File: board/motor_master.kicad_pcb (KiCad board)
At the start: 2 copper layers, 42 x 52 mm, 38 parts, among them IC1 LM1117MPX-3.3_NOPB, IC2 SN65HVD232DR, J1 PWR, J2 USB4105-GF-A, J3 FTDI, J4 CAN, J5 TERM, J6 PWM1, J7 PWM2, U1 ESP32-S3-WROOM-1-N8

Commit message: Board revisions from design review
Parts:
- added C13: 0.1uF, Capacitor_SMD:C_0603_1608Metric, F.Cu at (167.5, 122.0)
- added C14: 4.7n, Capacitor_SMD:C_0603_1608Metric, F.Cu at (167.5, 106.5)
- added C15: 100p, Capacitor_SMD:C_0603_1608Metric, F.Cu at (170.0, 106.0)
- added C9: 100p, Capacitor_SMD:C_0603_1608Metric, F.Cu at (165.0, 106.0)
- added D5: 150060RS75000, SamacSys_Parts:LEDC1608X80N, F.Cu at (171.5, 113.5)
- added D6: SZNUP2105LT1G, SamacSys_Parts:SOT96P237X111-3N, F.Cu at (167.5, 103.0)
- added J1: EXT, SamacSys_Parts:TSW-102-XX-YY-S, F.Cu at (128.8, 84.2)
- added R10: 47, Resistor_SMD:R_0603_1608Metric, F.Cu at (171.5, 118.2)
- added R2: 10k, Resistor_SMD:R_0603_1608Metric, F.Cu at (132.0, 82.0)
- added REF**: MountingHole_2.2mm_M2_Pad, MountingHole:MountingHole_2.2mm_M2_Pad, F.Cu at (170.0, 77.0)
- added REF**: MountingHole_2.2mm_M2_Pad, MountingHole:MountingHole_2.2mm_M2_Pad, F.Cu at (130.0, 125.5)
- added REF**: MountingHole_2.2mm_M2_Pad, MountingHole:MountingHole_2.2mm_M2_Pad, F.Cu at (130.0, 77.0)
- added REF**: MountingHole_2.2mm_M2_Pad, MountingHole:MountingHole_2.2mm_M2_Pad, F.Cu at (170.0, 125.5)
- D2: renamed from D3; value D5V0S1U2LP-7B -> PTVS18VU1UPAZ; footprint SamacSys_Parts:D5V0S1U2LP7B -> SamacSys_Parts:PMEG6020EPA115
- D4: value D5V0S1U2LP-7B -> PTVS18VU1UPAZ; footprint SamacSys_Parts:D5V0S1U2LP7B -> SamacSys_Parts:PMEG6020EPA115
- J4, J6, J7: footprint SamacSys_Parts:TSW-103-XX-YY-S -> SamacSys_Parts:1719710103
- J5: renamed from J1; value PWR -> 5-12V; footprint SamacSys_Parts:SHDR2W70P0X500_1X2_1000X750X1160P -> SamacSys_Parts:1190297
- J8: renamed from J5; footprint SamacSys_Parts:RHDR3W79P0X254_1X3_813X241X851P -> SamacSys_Parts:1719710103
- R1: renamed from R3; value 5.1k -> 47
- R8: value 10k -> 60; footprint Resistor_SMD:R_0603_1608Metric -> Resistor_SMD:R_1206_3216Metric
- R9: renamed from R7; value 120 -> 60; footprint Resistor_SMD:R_0603_1608Metric -> Resistor_SMD:R_1206_3216Metric
- moved IC2 41.1 mm to (167.5, 117.0), turned to 90 degrees
- moved R9 38.6 mm to (166.0, 110.5), turned to -90 degrees
- moved R11 38.5 mm to (167.8, 81.0), turned to 180 degrees
- moved R1 33.9 mm to (131.0, 120.5), turned to 90 degrees
- moved J8 32.7 mm to (164.9, 86.5), turned to 180 degrees
- moved J4 30.3 mm to (165.0, 95.5), turned to 180 degrees
- moved R8 29.6 mm to (169.0, 110.5), turned to -90 degrees
- moved D1 28.6 mm to (134.5, 125.5), turned to -90 degrees
- moved S4 27.0 mm to (162.0, 79.0)
- moved C7 26.2 mm to (137.4, 86.3)
- moved C11 23.5 mm to (158.5, 83.5), turned to 180 degrees
- moved J2 20.4 mm to (161.5, 116.0), turned to 90 degrees
- moved S1 20.0 mm to (136.0, 79.2), turned to -90 degrees
- moved R7 19.7 mm to (158.5, 85.5), turned to 0 degrees
- moved R6 16.4 mm to (160.5, 101.5), turned to -90 degrees
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- renumbered C2 to C1, C11 to C10, C8 to C11, C9 to C12, C1 to C2, C7 to C3, C6 to C4, C4 to C5, C5 to C6, C10 to C7, C3 to C8, D2 to D3, J3 to J2, J2 to J3, R6 to R11, R2 to R3, R1 to R4, R9 to R6, R4 to R7, S4 to S1, S3 to S2, S1 to S3, S2 to S4
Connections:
- C11 pad 2: GPIO15 -> GPIO48
- C7 pad 2: GPIO4 -> GPIO2
- D2 pad 1: VCC_IN -> Net-(D2-A_1)
- D2 pad 2: Net-(D2-IO1) -> Net-(D2-A_1)
- D3 pad 1: Net-(D2-IO1) -> Net-(D2-A_1)
- D4 pad 1: VCC_IN -> Net-(D4-A_1)
- D4 pad 2: Net-(D4-A) -> Net-(D4-A_1)
- IC2 pad 1: GPIO12 -> GPIO9
- IC2 pad 4: GPIO13 -> GPIO10
- IC2 pad 6: Net-(IC2-CANL) -> Net-(D6-CANL)
- J2 pad 2: Net-(D4-A) -> Net-(D4-A_1)
- J3 pad A4_B9: Net-(D2-IO1) -> Net-(D2-A_1)
- J3 pad B4_A9: Net-(D2-IO1) -> Net-(D2-A_1)
- J4 pad 2: unconnected-(J4-NC-Pad2) -> GND
- J4 pad 3: Net-(IC2-CANL) -> Net-(D6-CANL)
- J5 pad 2: GND -> VCC_IN
- J6 pad 1: GPIO5 -> GPIO21
- J7 pad 1: GPIO6 -> GPIO47
- J8 pad 2: unconnected-(J5-NC-Pad2) -> GND
- R7 pad 1: GPIO15 -> GPIO48
- R8 pad 1: GPIO4 -> Net-(C14-Pad2)
- R8 pad 2: VCC_3V3 -> Net-(D6-CANL)
- R9 pad 1: Net-(IC2-CANL) -> Net-(C14-Pad2)
- S1 pad 2: GPIO4 -> GPIO2
- S4 pad 2: GPIO15 -> GPIO48
- S4 pad 4: GPIO15 -> GPIO48
- U1 pad 17: unconnected-(U1-IO9-Pad17) -> GPIO9
- U1 pad 18: unconnected-(U1-IO10-Pad18) -> GPIO10
- U1 pad 19: unconnected-(U1-IO11-Pad19) -> GPIO11
- U1 pad 20: GPIO12 -> unconnected-(U1-IO12-Pad20)
- U1 pad 21: GPIO13 -> unconnected-(U1-IO13-Pad21)
- U1 pad 23: unconnected-(U1-IO21-Pad23) -> GPIO21
- U1 pad 24: unconnected-(U1-IO47-Pad24) -> GPIO47
- U1 pad 25: unconnected-(U1-IO48-Pad25) -> GPIO48
- U1 pad 38: unconnected-(U1-IO2-Pad38) -> GPIO2
- U1 pad 39: unconnected-(U1-IO1-Pad39) -> GPIO1
- U1 pad 4: GPIO4 -> unconnected-(U1-IO4-Pad4)
- U1 pad 5: GPIO5 -> unconnected-(U1-IO5-Pad5)
- U1 pad 6: GPIO6 -> unconnected-(U1-IO6-Pad6)
- U1 pad 8: GPIO15 -> unconnected-(U1-IO15-Pad8)
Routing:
- net GPIO4: track 42.3 -> 0.00 mm, vias 2 -> 0
- net GPIO5: track 40.3 -> 0.00 mm, vias 1 -> 0
- net GPIO6: track 31.6 -> 0.00 mm, vias 1 -> 0
- net GPIO10: track 0.00 -> 31.1 mm
- net GPIO11: track 0.00 -> 29.6 mm, vias 0 -> 2
- net GPIO9: track 0.00 -> 26.5 mm
- net GPIO15: track 23.9 -> 0.00 mm, vias 1 -> 0
- net GPIO13: track 21.4 -> 0.00 mm, vias 2 -> 0
- net Net-(D6-CANL): track 0.00 -> 21.3 mm
- net VCC_IN: track 28.9 -> 48.8 mm, vias 0 -> 2
- net GPIO21: track 0.00 -> 18.9 mm, vias 0 -> 2
- net GPIO48: track 0.00 -> 18.9 mm
- net GPIO12: track 17.3 -> 0.00 mm, vias 2 -> 0
- net Net-(D2-IO1): track 17.1 -> 0.00 mm, vias 2 -> 0
- net Net-(D2-A_1): track 0.00 -> 15.1 mm, vias 0 -> 2
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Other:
- board size 42 x 52 mm -> 47 x 55.5 mm
- rule pad_to_mask_clearance: 0.038 -> 0.0508
- board text added: "+"
- board text added: "-"
- board text added: "47x55.5mm"
- board text added: "5-12v"
- board text added: "G"
- board text added: "Robotics Academy 2024 v1"
- board text added: "S"

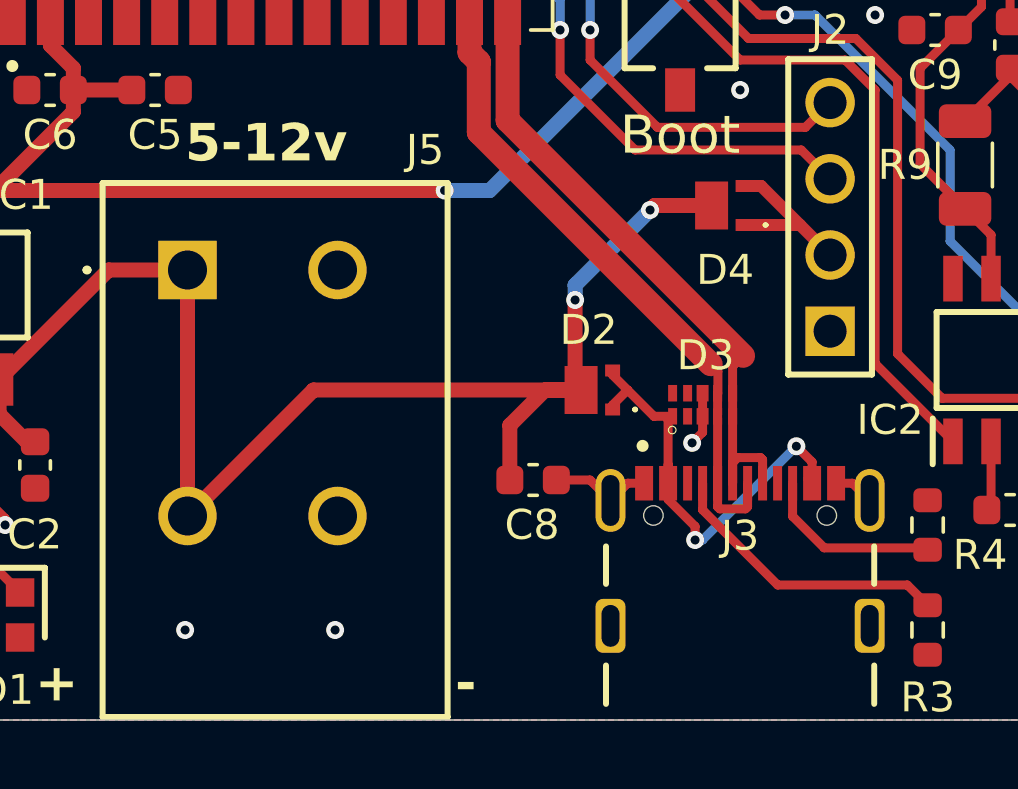
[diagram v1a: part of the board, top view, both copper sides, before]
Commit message: Changed power diodes
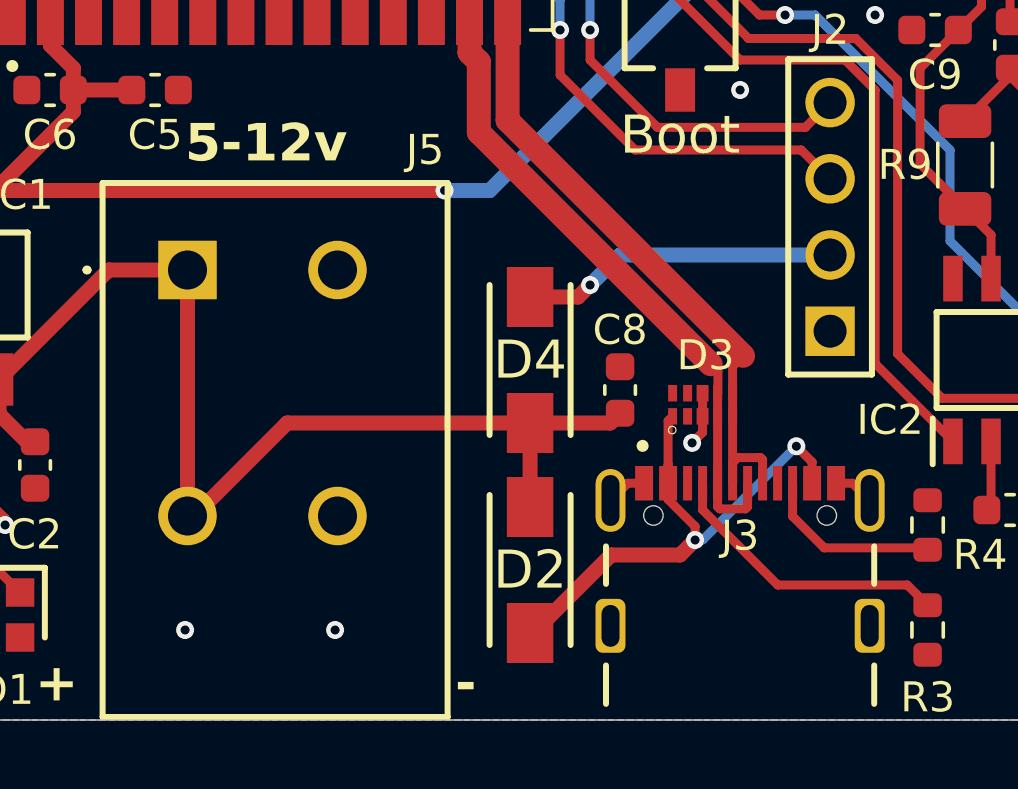
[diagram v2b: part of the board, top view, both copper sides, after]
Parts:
- D2, D4: value PTVS18VU1UPAZ -> SK14; footprint SamacSys_Parts:PMEG6020EPA115 -> SamacSys_Parts:DIONM5027X250N
- moved D4 8.14 mm to (151.5, 117.0)
- moved D2 6.31 mm to (151.5, 124.0), turned to -90 degrees
- moved C8 4.17 mm to (154.5, 118.0), turned to -90 degrees
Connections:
- D2 pad 1: Net-(D2-A_1) -> VCC_IN
- D2 pad 2: Net-(D2-A_1) -> Net-(D2-A)
- D3 pad 1: Net-(D2-A_1) -> Net-(D2-A)
- D4 pad 1: Net-(D4-A_1) -> VCC_IN
- D4 pad 2: Net-(D4-A_1) -> Net-(D4-A)
- J2 pad 2: Net-(D4-A_1) -> Net-(D4-A)
- J3 pad A4_B9: Net-(D2-A_1) -> Net-(D2-A)
- J3 pad B4_A9: Net-(D2-A_1) -> Net-(D2-A)
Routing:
- net Net-(D2-A): track 0.00 -> 18.3 mm, vias 0 -> 2
- net Net-(D2-A_1): track 15.1 -> 0.00 mm, vias 2 -> 0
- net Net-(D4-A): track 0.00 -> 10.6 mm, vias 0 -> 1
- net VCC_IN: track 48.8 -> 38.6 mm, vias 2 -> 0
- net Net-(D4-A_1): track 7.17 -> 0.00 mm
- net GND: track 23.2 -> 21.1 mm

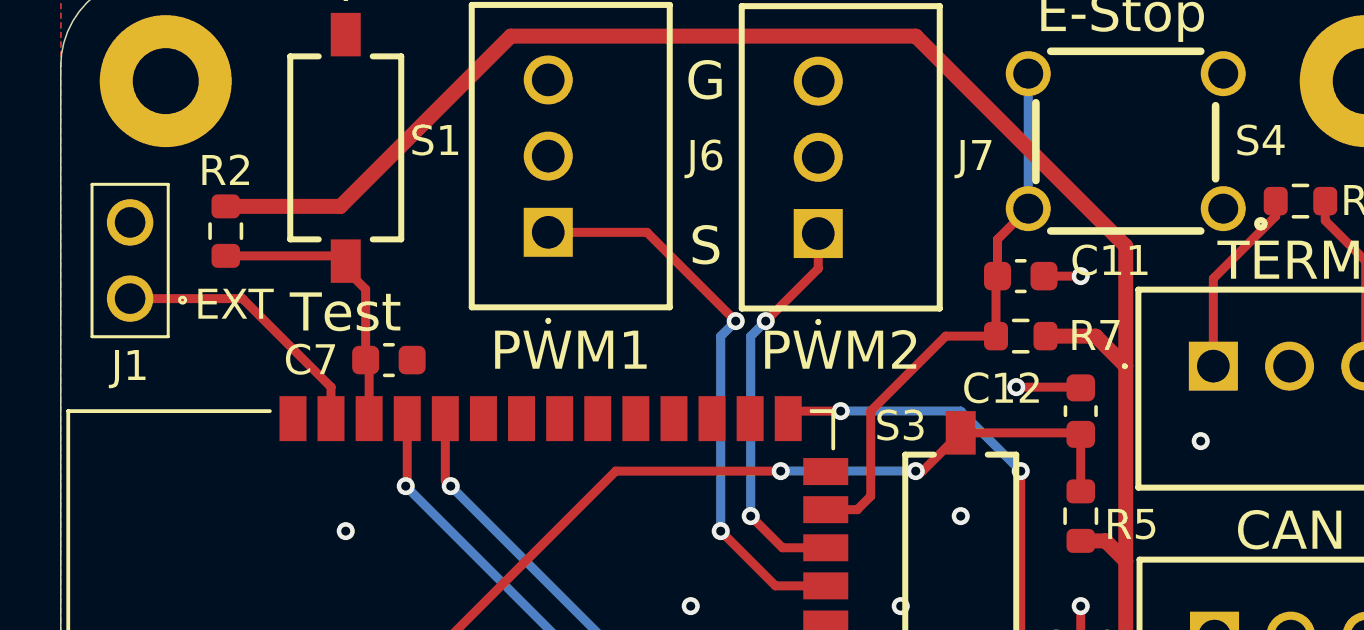
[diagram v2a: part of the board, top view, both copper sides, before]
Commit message: Updated BOM with manufactuer numbers
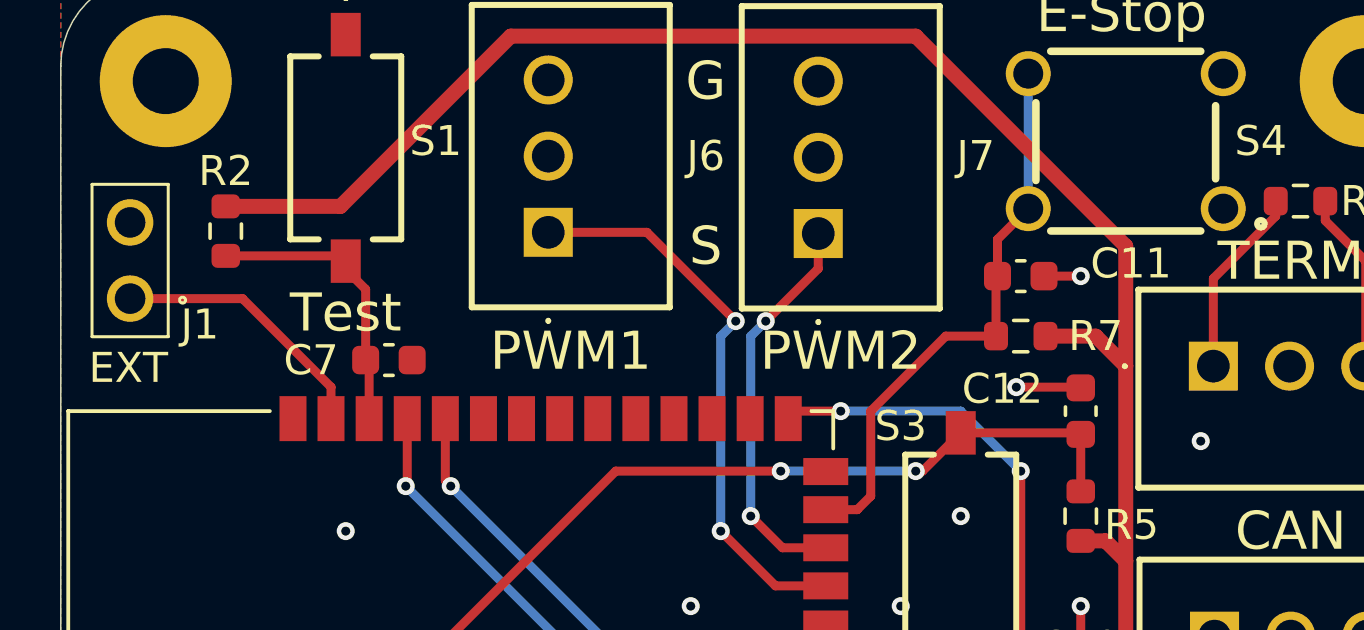
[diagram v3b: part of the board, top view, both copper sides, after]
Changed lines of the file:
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@@
 			(outputformat 1)
 			(mirror no)
-			(drillshape 1)
+			(drillshape 0)
 			(scaleselection 1)
-			(outputdirectory "")
+			(outputdirectory "gerber")
 		)
 	)
@@
 		(tags "Connector")
 		(property "Reference" "J1"
-			(at -2.25 0 180)
+			(at -0.865071 2.324069 180)
 			(layer "F.SilkS")
 			(effects
@@
 		)
 		(property "Value" "EXT"
-			(at -0.206986 3.462927 180)
+			(at -2.311707 -0.057316 180)
 			(layer "F.SilkS")
 			(effects
@@
 		(tags "capacitor")
 		(property "Reference" "C11"
-			(at -3 0.5 180)
+			(at -3.675096 0.418395 180)
 			(layer "F.SilkS")
 			(effects
@@
 		(tags "Diode")
 		(property "Reference" "D2"
-			(at 0 0 360)
+			(at 0 0 0)
 			(layer "F.SilkS")
 			(effects
@@
 		(tags "capacitor")
 		(property "Reference" "C8"
-			(at -2 0 360)
+			(at -2 0 0)
 			(layer "F.SilkS")
 			(effects
@@
 	)
 	(gr_text "47x55.5mm"
-		(at 138.272576 103.789211 90)
+		(at 138.272576 105 90)
 		(layer "B.SilkS")
 		(effects

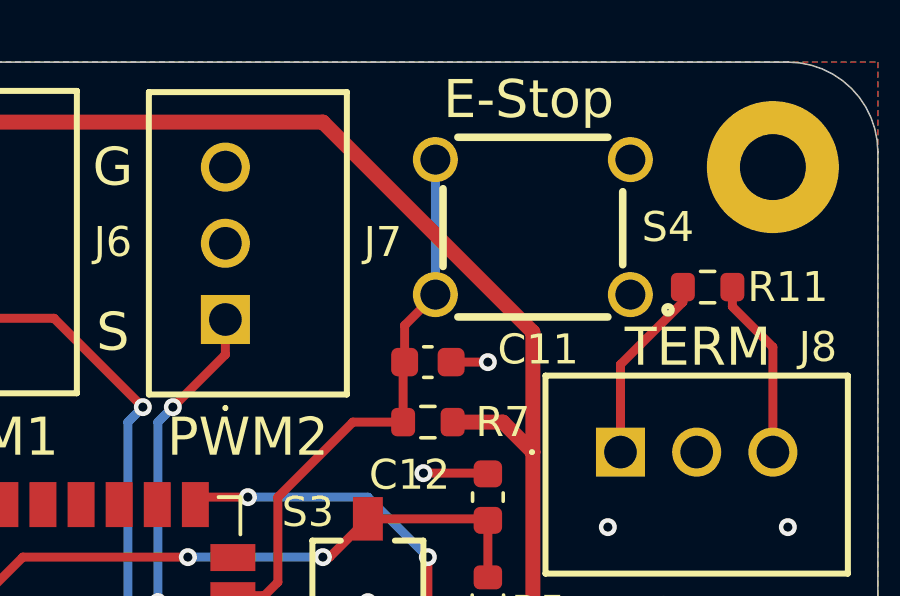
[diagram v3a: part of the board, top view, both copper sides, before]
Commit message: Changed LEDs and fixed estop button wiring
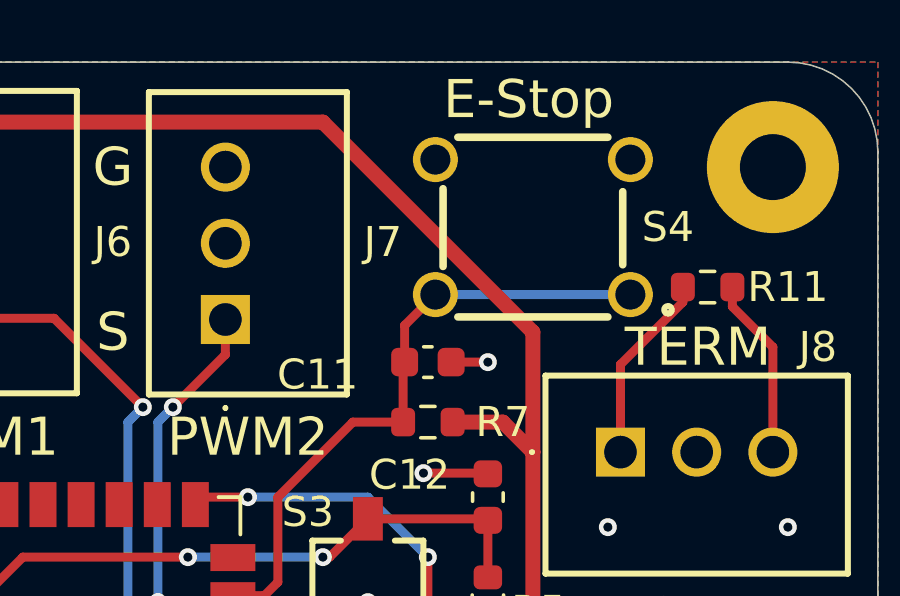
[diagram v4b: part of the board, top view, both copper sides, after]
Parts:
- R1, R10: value 47 -> 100
- turned C11 to 0 degrees
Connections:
- C11 pad 1: GND -> GPIO48
- C11 pad 2: GPIO48 -> GND
- S4 pad 1: GND -> GPIO48
- S4 pad 4: GPIO48 -> GND
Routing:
- net GPIO48: track 18.9 -> 20.9 mm

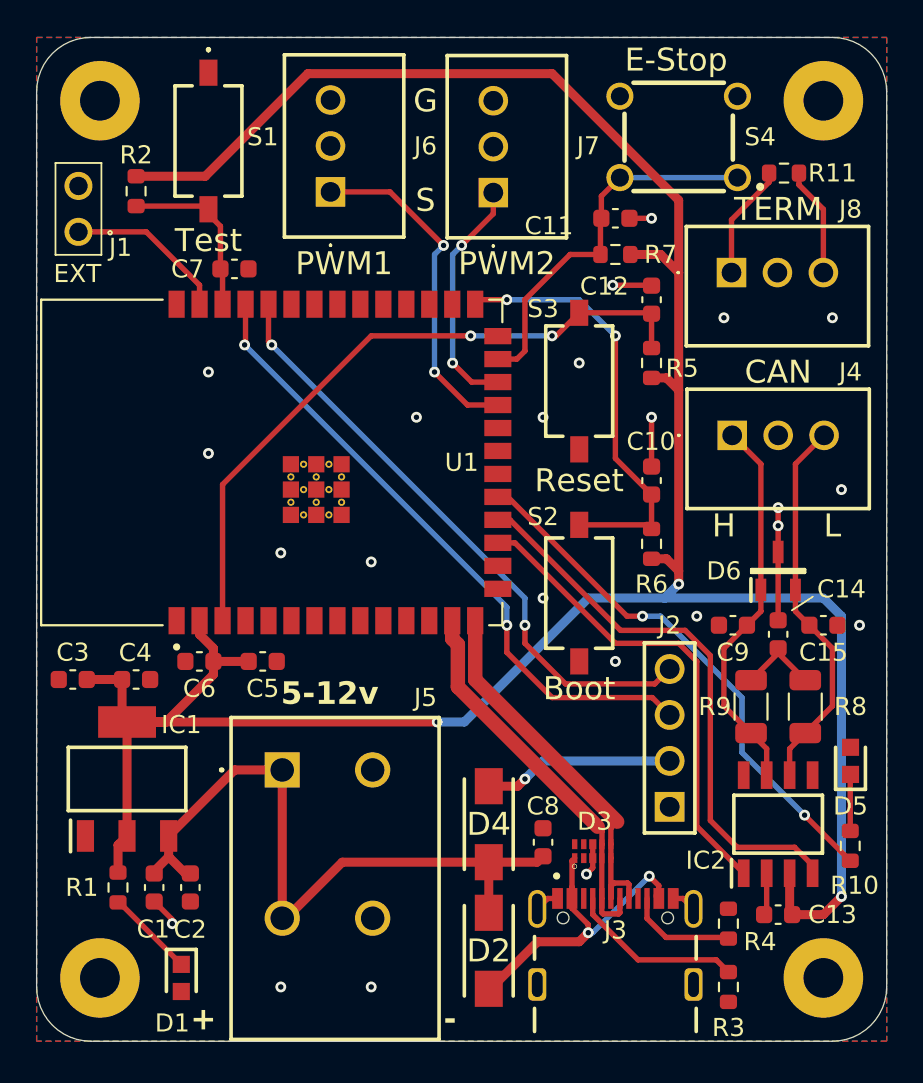
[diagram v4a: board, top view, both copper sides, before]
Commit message: Added pullup resistor to extern pin, renumbered parts
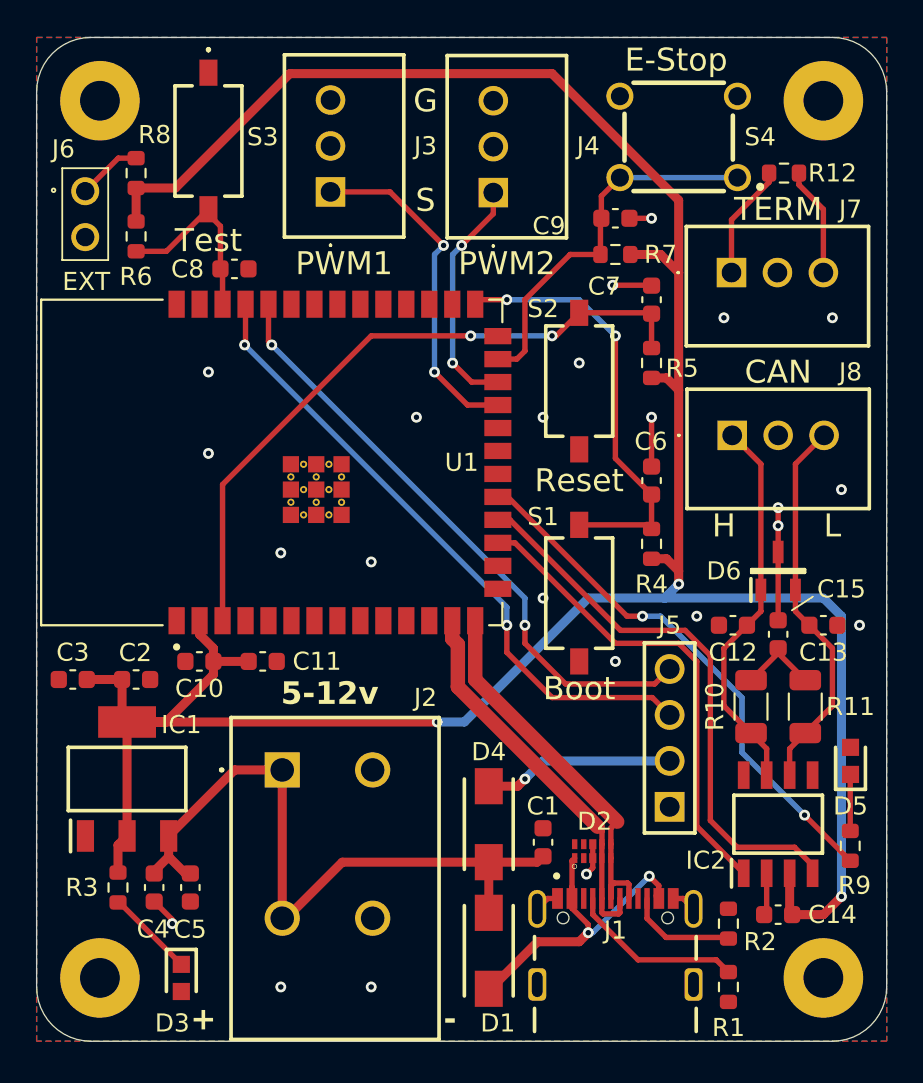
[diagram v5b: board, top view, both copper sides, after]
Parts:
- added R8: 10k, Resistor_SMD:R_0603_1608Metric, F.Cu at (132.0, 81.0)
- moved R6 2.50 mm to (132.0, 84.5)
- moved J6 2.28 mm to (129.2, 82.0), turned to -90 degrees
- renumbered C8 to C1, C6 to C10, C5 to C11, C9 to C12, C15 to C13, C13 to C14, C14 to C15, C4 to C2, C1 to C4, C2 to C5, C10 to C6, C12 to C7, C7 to C8, C11 to C9, D2 to D1, D3 to D2, D1 to D3, J3 to J1, J5 to J2, J6 to J3, J7 to J4, J2 to J5, J1 to J6, J8 to J7, J4 to J8, R3 to R1, R9 to R10, R8 to R11, R11 to R12, R4 to R2, R1 to R3, R6 to R4, R2 to R6, R10 to R9, S2 to S1, S3 to S2, S1 to S3
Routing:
- net GPIO1: track 8.97 -> 3.57 mm
- net VCC_3V3: track 152.0 -> 154.1 mm
- net GPIO2: track 9.65 -> 10.8 mm
